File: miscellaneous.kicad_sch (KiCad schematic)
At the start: 0 parts

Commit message: Fixed net labels and added Ethernet reset digital logic. Also continued to update pinmux on TI sysconfig
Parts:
- added D801, D802: LED, symbol Device:LED
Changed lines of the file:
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@@
 	(generator_version "9.0")
 	(paper "A3")
+	(symbol
+		(lib_id "Device:LED")
+		(at 113.03 67.31 90)
+		(unit 1)
+		(exclude_from_sim no)
+		(in_bom yes)
+		(on_board yes)
+		(dnp no)
+		(fields_autoplaced yes)
+		(property "Reference" "D802"
+			(at 116.84 67.6274 90)
+			(effects
+				(font
+					(size 1.27 1.27)
+				)
+				(justify right)
+			)
+		)
+		(property "Value" "LED"
+			(at 116.84 70.1674 90)
+			(effects
+				(font
+					(size 1.27 1.27)
+				)
+				(justify right)
+			)
+		)
+		(property "Footprint" ""
+			(at 113.03 67.31 0)
+			(effects
+				(font
+					(size 1.27 1.27)
+				)
+				(hide yes)
+			)
+		)
+		(property "Datasheet" "~"
+			(at 113.03 67.31 0)
+			(effects
+				(font
+					(size 1.27 1.27)
+				)
+				(hide yes)
+			)
+		)
+		(property "Description" "Light emitting diode"
+			(at 113.03 67.31 0)
+			(effects
+				(font
+					(size 1.27 1.27)
+				)
+				(hide yes)
+			)
+		)
+		(property "Sim.Pins" "1=K 2=A"
+			(at 113.03 67.31 0)
+			(effects
+				(font
+					(size 1.27 1.27)
+				)
+				(hide yes)
+			)
+		)
+		(pin "1"
+		)
+		(pin "2"
+		)
+		(instances
+			(project "Leonhart"
+				(path "/b43b7bca-e50d-42ec-8ff0-e0016dfefe0a/5ce8c427-fcc7-46d6-9710-77fc43565e4a"
+					(reference "D802")
+					(unit 1)
+				)
+			)
+		)
+	)
+	(symbol
+		(lib_id "Device:LED")
+		(at 99.06 67.31 90)
+		(unit 1)
+		(exclude_from_sim no)
+		(in_bom yes)
+		(on_board yes)
+		(dnp no)
+		(fields_autoplaced yes)
+		(property "Reference" "D801"
+			(at 102.87 67.6274 90)
+			(effects
+				(font
+					(size 1.27 1.27)
+				)
+				(justify right)
+			)
+		)
+		(property "Value" "LED"
+			(at 102.87 70.1674 90)
+			(effects
+				(font
+					(size 1.27 1.27)
+				)
+				(justify right)
+			)
+		)
+		(property "Footprint" ""
+			(at 99.06 67.31 0)
+			(effects
+				(font
+					(size 1.27 1.27)
+				)
+				(hide yes)
+			)
+		)
+		(property "Datasheet" "~"
+			(at 99.06 67.31 0)
+			(effects
+				(font
+					(size 1.27 1.27)
+				)
+				(hide yes)
+			)
+		)
+		(property "Description" "Light emitting diode"
+			(at 99.06 67.31 0)
+			(effects
+				(font
+					(size 1.27 1.27)
+				)
+				(hide yes)
+			)
+		)
+		(property "Sim.Pins" "1=K 2=A"
+			(at 99.06 67.31 0)
+			(effects
+				(font
+					(size 1.27 1.27)
+				)
+				(hide yes)
+			)
+		)
+		(pin "1"
+		)
+		(pin "2"
+		)
+		(instances
+			(project ""
+				(path "/b43b7bca-e50d-42ec-8ff0-e0016dfefe0a/5ce8c427-fcc7-46d6-9710-77fc43565e4a"
+					(reference "D801")
+					(unit 1)
+				)
+			)
+		)
+	)
 )

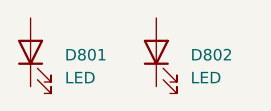
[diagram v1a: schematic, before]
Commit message: Fixed SoC power circuitry
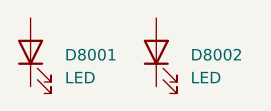
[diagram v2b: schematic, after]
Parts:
- renumbered D801 to D8001, D802 to D8002
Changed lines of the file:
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@@
 		(dnp no)
 		(fields_autoplaced yes)
-		(property "Reference" "D802"
+		(property "Reference" "D8002"
 			(at 116.84 67.6274 90)
 			(effects
@@
 			(project "Leonhart"
 				(path "/b43b7bca-e50d-42ec-8ff0-e0016dfefe0a/5ce8c427-fcc7-46d6-9710-77fc43565e4a"
-					(reference "D802")
+					(reference "D8002")
 					(unit 1)
 				)
@@
 		(dnp no)
 		(fields_autoplaced yes)
-		(property "Reference" "D801"
+		(property "Reference" "D8001"
 			(at 102.87 67.6274 90)
 			(effects
@@
 			(project ""
 				(path "/b43b7bca-e50d-42ec-8ff0-e0016dfefe0a/5ce8c427-fcc7-46d6-9710-77fc43565e4a"
-					(reference "D801")
+					(reference "D8001")
 					(unit 1)
 				)

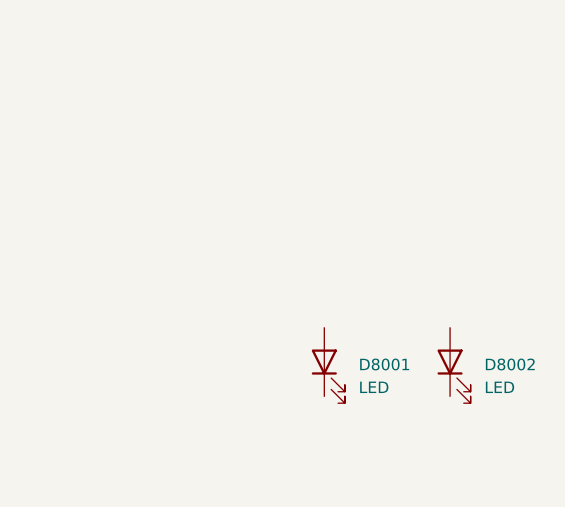
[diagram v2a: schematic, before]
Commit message: Finished overall schematic. Fixing errors and warnings from ERC
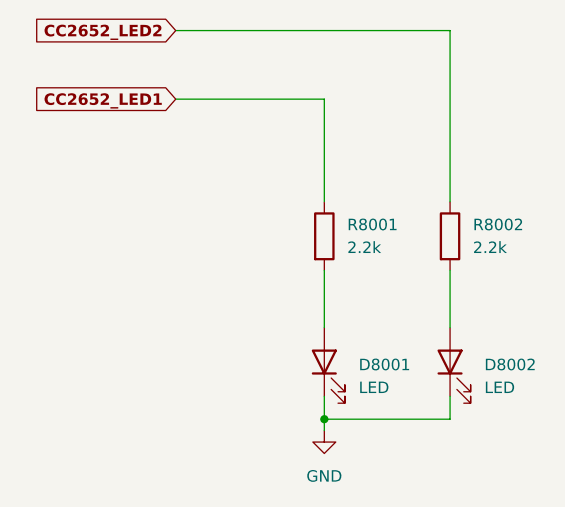
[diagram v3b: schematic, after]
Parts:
- added R8001, R8002: 2.2k, symbol Device:R
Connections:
- net GND: now reaches D8002.1 (K)
- net GND: now also D8001.1 (K)
- net at D8002.2 (A): now also R8002.2
- net at D8001.2 (A): now also R8001.2
- new net CC2652_LED1: R8001.1
- new net CC2652_LED2: R8002.1

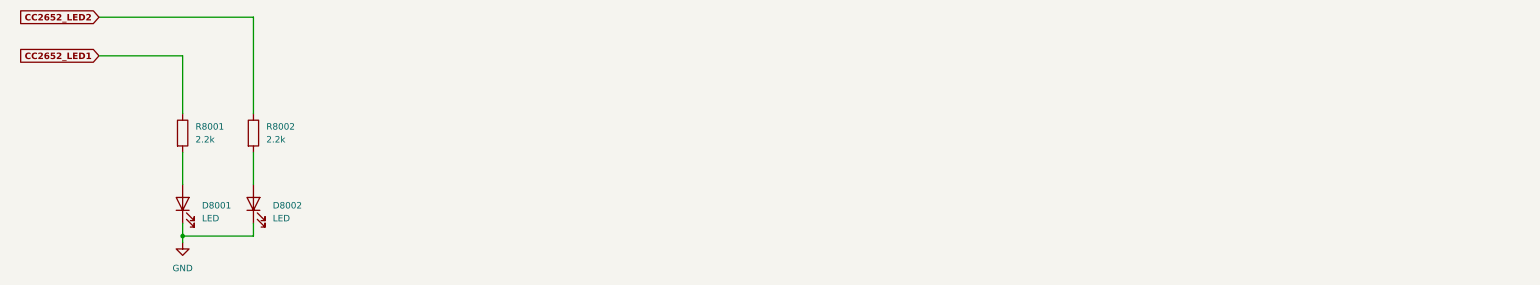
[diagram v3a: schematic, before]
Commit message: Double checked power, ddr4, USB, MMC and added bootstrap. Also added buttons and added pinmuxing in sysconfig
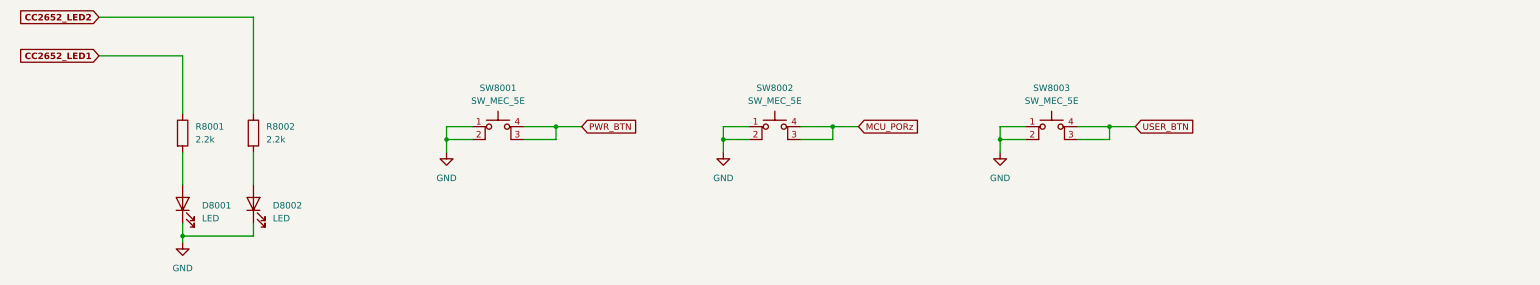
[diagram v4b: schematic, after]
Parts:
- added SW8001, SW8002, SW8003: SW_MEC_5E, symbol Switch:SW_MEC_5E
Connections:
- net GND: now also SW8001.1, SW8001.2, SW8002.1, SW8002.2, SW8003.1, SW8003.2
- new net MCU_PORz: SW8002.3 (K), SW8002.4 (A)
- new net PWR_BTN: SW8001.3 (K), SW8001.4 (A)
- new net USER_BTN: SW8003.3 (K), SW8003.4 (A)

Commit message: Added almost all passive component footprints
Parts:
- R8001, R8002: footprint (none) -> Resistor_SMD:R_0402_1005Metric
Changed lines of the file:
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@@
 			)
 		)
-		(property "Footprint" ""
+		(property "Footprint" "Resistor_SMD:R_0402_1005Metric"
 			(at 97.282 53.34 90)
 			(effects
@@
 			)
 		)
-		(property "Footprint" ""
+		(property "Footprint" "Resistor_SMD:R_0402_1005Metric"
 			(at 111.252 53.34 90)
 			(effects

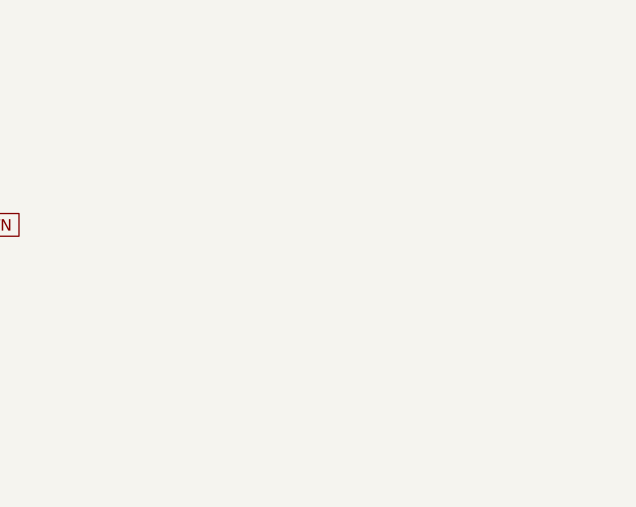
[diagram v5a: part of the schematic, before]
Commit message: Switched out CC2652P and nRF52840 for MGM240P to run Zigbee and Thread
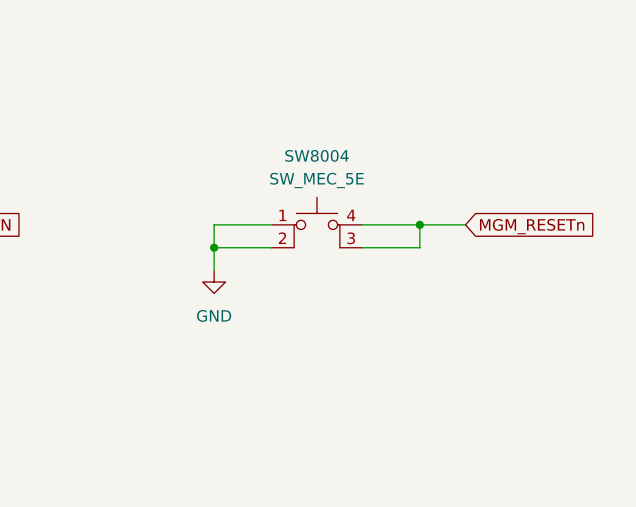
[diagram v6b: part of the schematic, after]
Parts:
- added SW8004: SW_MEC_5E, symbol Switch:SW_MEC_5E
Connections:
- net GND: now also SW8004.1, SW8004.2
- new net MGM_RESETn: SW8004.3 (K), SW8004.4 (A)

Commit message: Added new radio schematic
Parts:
- removed D8001, D8002: LED, symbol Device:LED
- removed R8001, R8002: 2.2k, Resistor_SMD:R_0402_1005Metric, symbol Device:R
- renumbered SW8001 to SW7001, SW8002 to SW7002, SW8003 to SW7003, SW8004 to SW7004

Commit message: Placed ferrite beads and relevant decoupling caps for analog 1.8V rails
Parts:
- SW7001, SW7002, SW7003, SW7004: footprint (none) -> SoftServicesFootprintLibrary:1825910-6
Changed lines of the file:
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@@
 			)
 		)
-		(property "Footprint" ""
+		(property "Footprint" "SoftServicesFootprintLibrary:1825910-6"
 			(at 270.51 46.99 0)
 			(effects
@@
 			)
 		)
-		(property "Footprint" ""
+		(property "Footprint" "SoftServicesFootprintLibrary:1825910-6"
 			(at 331.47 46.99 0)
 			(effects
@@
 			)
 		)
-		(property "Footprint" ""
+		(property "Footprint" "SoftServicesFootprintLibrary:1825910-6"
 			(at 215.9 46.99 0)
 			(effects
@@
 			)
 		)
-		(property "Footprint" ""
+		(property "Footprint" "SoftServicesFootprintLibrary:1825910-6"
 			(at 161.29 46.99 0)
 			(effects
